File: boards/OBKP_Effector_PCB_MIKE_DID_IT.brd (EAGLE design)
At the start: 66.9 x 57.9 mm, 34 parts

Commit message: put fan vcc (12v!) on separate pin from led vcc (5v)
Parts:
- moved PROBE+ 0.22 mm to (58.0, 31.9)
- moved PROBE- 0.14 mm to (47.9, 49.1)
- renumbered HOTHEDR to HOT_HEADER
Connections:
- new net N$15: FAN_VCC+.P$1, HOT_HEADER.1
- net FAN_VCC: now also HOT_HEADER.3; no longer FAN_VCC+.P$1, HOT_HEADER.1
- net N$11: now also HOT_HEADER.8; no longer HOT_HEADER.4
- net N$19: now also HOT_HEADER.4; no longer HOT_HEADER.3
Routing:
- net FAN_VCC: track 159.4 -> 108.4 mm
- net N$15: track 0.00 -> 14.7 mm
- net N$19: track 38.6 -> 40.6 mm
- net N$11: track 58.7 -> 57.0 mm

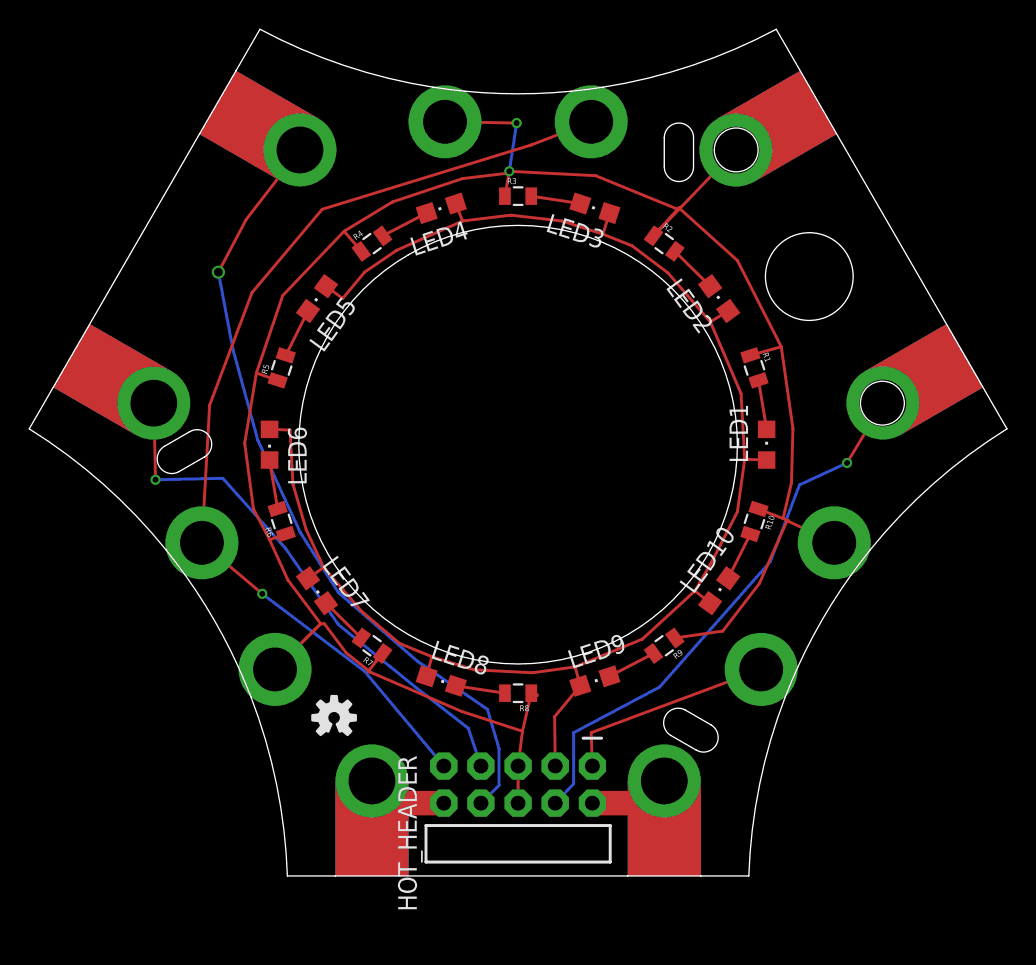
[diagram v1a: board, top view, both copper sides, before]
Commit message: put third fan pwm pin on same net as other two
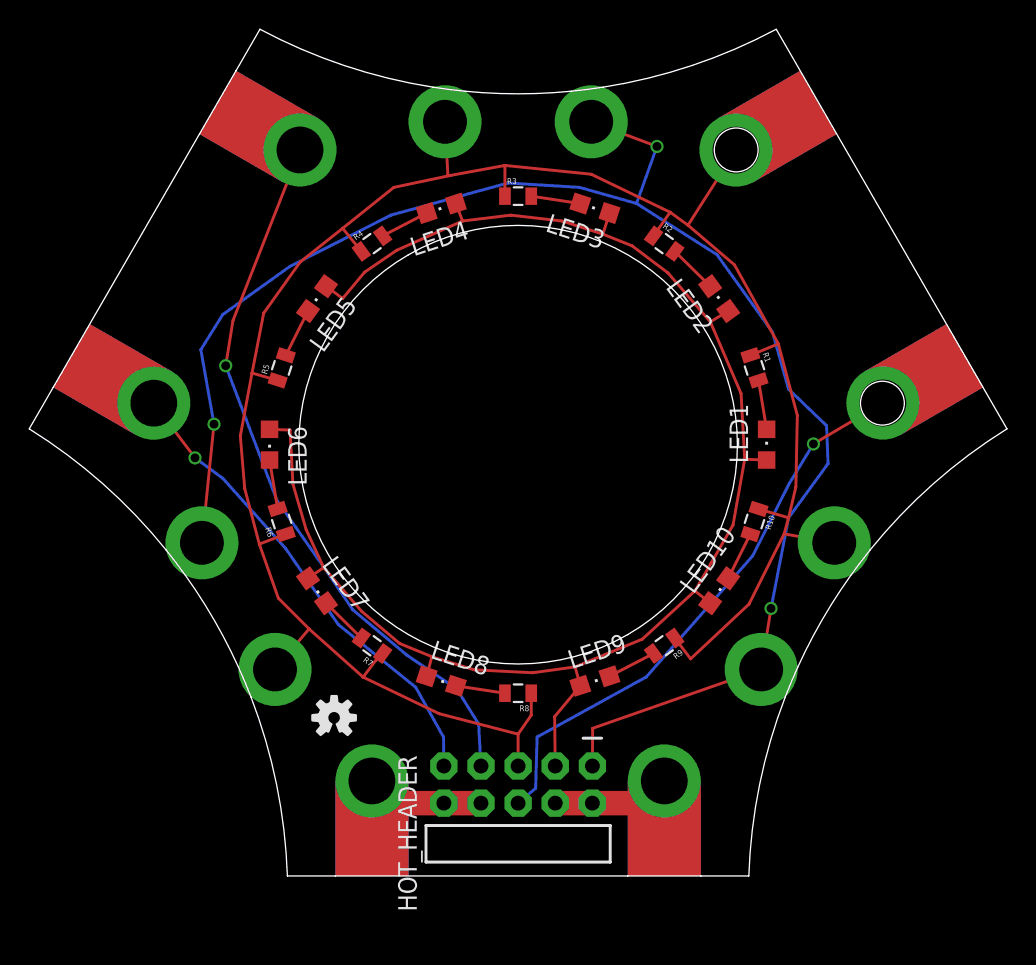
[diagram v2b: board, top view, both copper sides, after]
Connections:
- removed net N$12: FAN_PWM+.P$1, FAN_PWM2+.P$1, HOT_HEADER.9
- net GND: no longer HOT_HEADER.6
- net N$10: now also HOT_HEADER.8
- net N$11: now also HOT_HEADER.7; no longer HOT_HEADER.8
- net N$15: now also FAN_PWM+.P$1, FAN_PWM2+.P$1
- net N$19: now also HOT_HEADER.6; no longer HOT_HEADER.4
- net N$20: now also HOT_HEADER.9; no longer HOT_HEADER.7
- net N$8: now also HOT_HEADER.4
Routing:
- net N$15: track 14.7 -> 109.0 mm, vias 0 -> 3
- net N$12: track 67.1 -> 0.00 mm, vias 1 -> 0
- net GND: track 162.2 -> 151.0 mm, vias 2 -> 0
- net N$11: track 57.0 -> 52.5 mm
- net N$20: track 40.0 -> 35.8 mm
- net N$8: track 11.0 -> 13.6 mm
- net N$10: track 7.85 -> 10.4 mm
- net N$19: track 40.6 -> 42.1 mm
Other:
- outline, holes or cut-outs redrawn

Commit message: moved fan+ to hot+ net and fan- to fan pwm net and rerouted with burlier traces
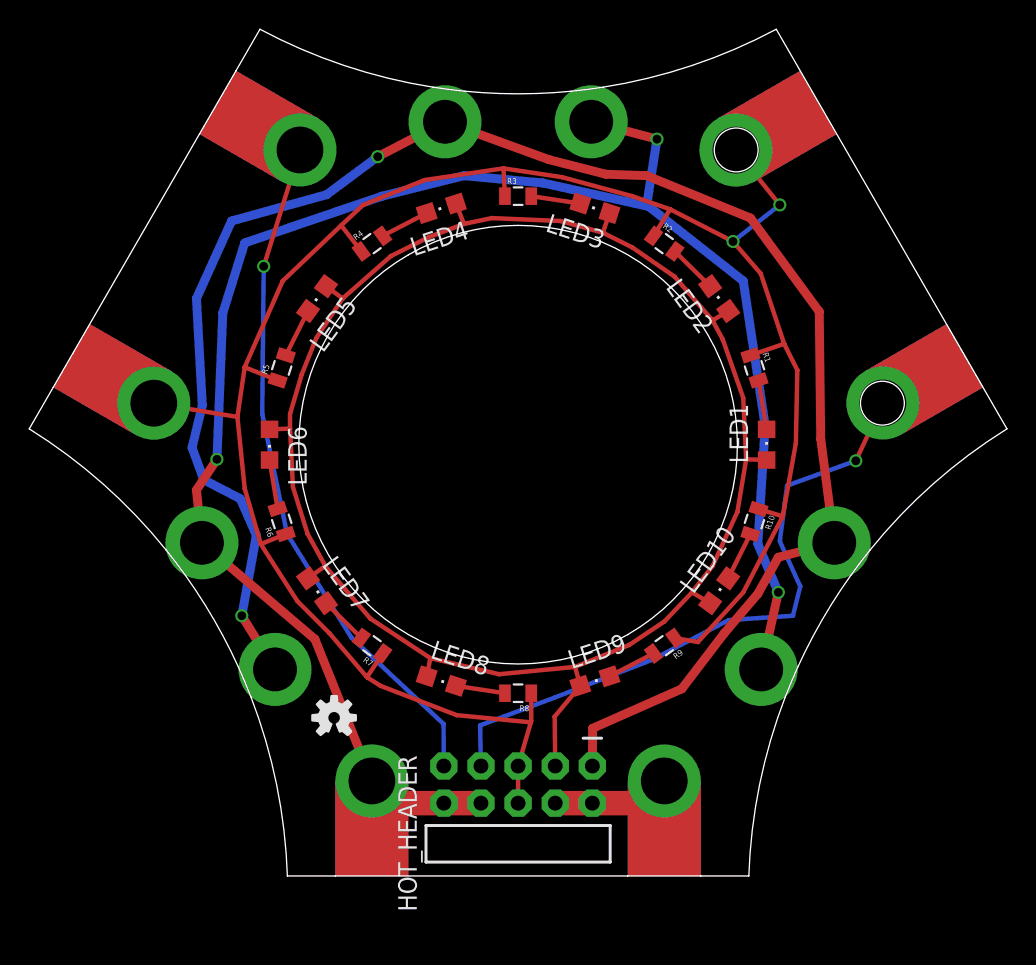
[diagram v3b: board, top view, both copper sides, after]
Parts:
- renumbered FAN_PWM+ to FAN_0_VCC, FAN_PWM- to FAN_1_PWM, FAN_PWM2+ to FAN_2_VCC, FAN_PWM2- to FAN_2_PWM, FAN_VCC+ to FAN_1_VCC, FAN_VCC- to FAN_0_PWM, HOT+ to HOT_VCC, HOT- to HOT_PWM
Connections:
- removed net N$15: FAN_0_VCC.P$1, FAN_1_VCC.P$1, FAN_2_VCC.P$1, HOT_HEADER.1
- removed net N$19: HOT_HEADER.6, PROBE+.P$1, PROBE+.P$2, PROBE+.P$3
- removed net N$20: HOT_HEADER.9, THERM-.P$1, THERM-.P$2, THERM-.P$3
- new net N$12: HOT_HEADER.7, PROBE+.P$1, PROBE+.P$2, PROBE+.P$3
- new net N$17: FAN_0_PWM.P$1, FAN_1_PWM.P$1, FAN_2_PWM.P$1, HOT_HEADER.1
- net GND: now also HOT_HEADER.6, THERM-.P$1, THERM-.P$2, THERM-.P$3; no longer FAN_0_PWM.P$1, FAN_1_PWM.P$1, FAN_2_PWM.P$1
- net N$10: now also FAN_0_VCC.P$1, FAN_1_VCC.P$1, FAN_2_VCC.P$1
- net N$11: now also HOT_HEADER.9; no longer HOT_HEADER.7
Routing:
- net N$17: track 0.00 -> 120.5 mm, vias 0 -> 2
- net N$10: track 10.4 -> 125.5 mm, vias 0 -> 3
- net N$15: track 109.0 -> 0.00 mm, vias 3 -> 0
- net N$12: track 0.00 -> 47.6 mm, vias 0 -> 1
- net N$19: track 42.1 -> 0.00 mm, vias 1 -> 0
- net N$20: track 35.8 -> 0.00 mm, vias 1 -> 0
- net FAN_VCC: track 108.4 -> 118.2 mm
- net GND: track 151.0 -> 154.0 mm, vias 0 -> 2
- net N$11: track 52.5 -> 49.9 mm

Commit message: cleaned up board
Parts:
- moved FAN_0_PWM 39.2 mm to (28.0, 51.1), turned to 0 degrees
- moved FAN_1_PWM 39.2 mm to (54.6, 22.3), turned to 330 degrees
- renumbered FAN_0_VCC to FAN_0_12V, FAN_1_VCC to FAN_1_12V, FAN_2_VCC to FAN_2_12V, HOT_VCC to HOT_12V, PROBE+ to PROBE_SIG, PROBE- to PROBE_GND, THERM+ to THERM_SIG, THERM- to THERM_GND
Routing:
- net N$15: track 13.6 -> 10.4 mm
